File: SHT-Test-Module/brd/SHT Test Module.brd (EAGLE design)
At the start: 38.1 x 38.1 mm, 13 parts

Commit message: Added SHT board files
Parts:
- moved U$11 35.1 mm to (34.2, 15.2)
- moved U$6 29.2 mm to (31.5, 16.9)
- moved U$7 24.5 mm to (21.8, 5.21), turned to 270 degrees
- moved U$8 21.0 mm to (7.24, 13.8), turned to 270 degrees
- moved U$5 19.7 mm to (22.9, 29.1), turned to 90 degrees
- moved U$9 12.9 mm to (7.24, 17.8)
- moved U$1 6.45 mm to (13.6, 15.6), turned to 0 degrees
- moved U$2 5.66 mm to (28.8, 27.4)
- moved U$3 5.66 mm to (28.8, 24.9)
- moved U$4 5.66 mm to (28.8, 22.4)
- moved U$12 5.53 mm to (28.8, 30.1)
- moved U$10 3.75 mm to (20.1, 14.9), turned to 270 degrees
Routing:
- net GND: track 95.7 -> 24.7 mm, vias 5 -> 8
- net DATA: track 38.2 -> 19.5 mm
- net CMD: track 8.35 -> 20.3 mm, vias 0 -> 2
- net PING: track 12.5 -> 20.7 mm
- net SCK: track 16.7 -> 8.52 mm, vias 0 -> 1
- net CLK: track 25.0 -> 19.2 mm
- net SDA: track 19.0 -> 13.4 mm, vias 2 -> 0
- net MISO: track 14.9 -> 9.78 mm
- net ALIVE: track 17.0 -> 22.0 mm, vias 0 -> 2
- net RESET: track 62.0 -> 59.8 mm, vias 1 -> 3
- net N$12: track 8.65 -> 6.94 mm
- net N$15: track 8.27 -> 6.99 mm
- net N$14: track 8.27 -> 6.99 mm
- net N$13: track 8.27 -> 6.99 mm
- net SCL: track 16.0 -> 16.9 mm
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- added copper zone on layer 16, net GND
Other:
- board size 38.1 x 38.1 mm -> 38.1 x 38.2 mm

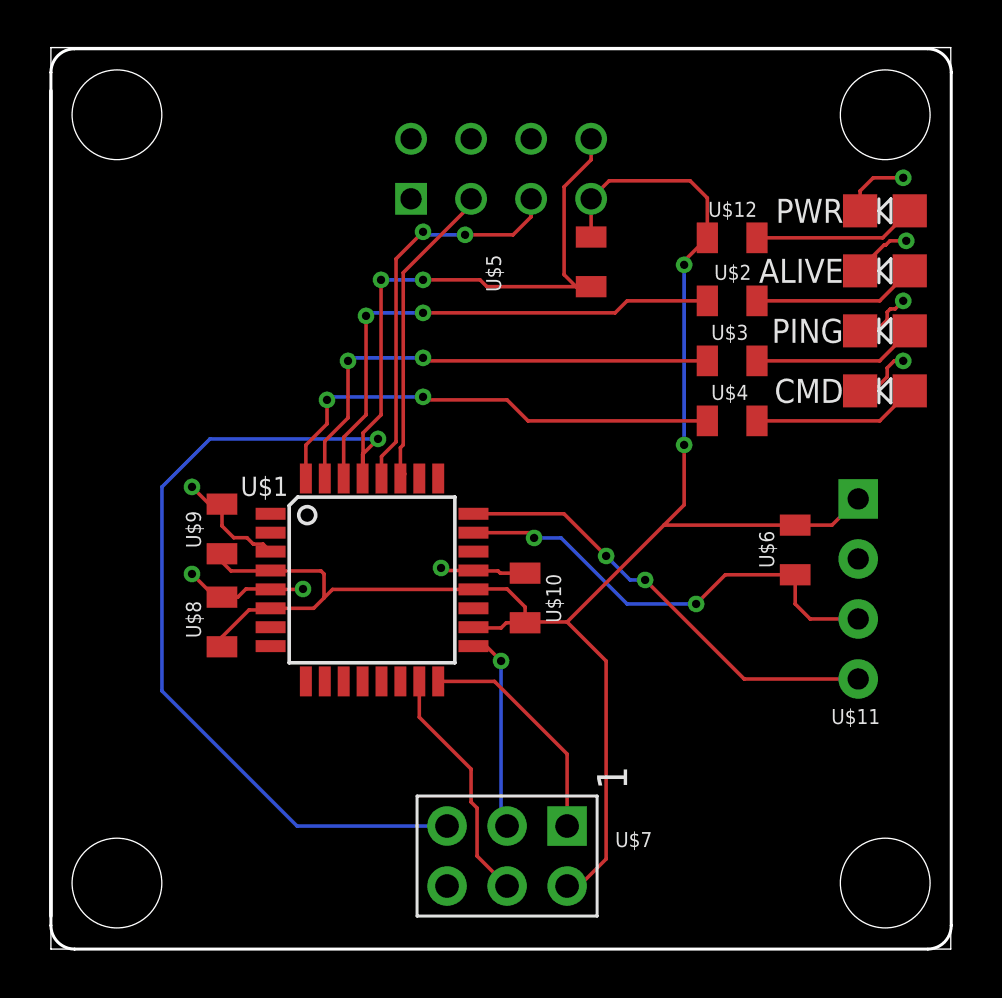
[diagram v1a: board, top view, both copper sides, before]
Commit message: updated board templates and modified existing boards to use the mk2 templates.
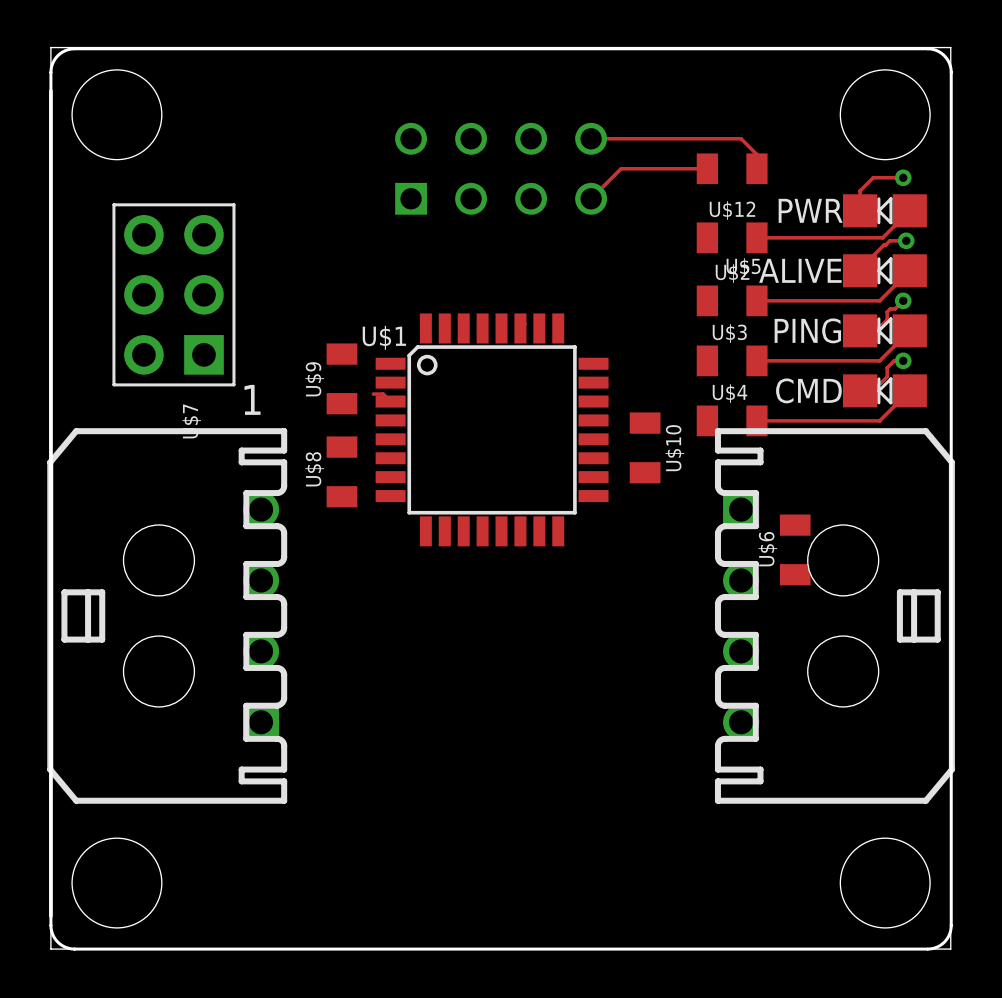
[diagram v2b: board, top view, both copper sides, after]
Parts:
- removed U$11: 4PIN-HEADER, 000_CustomPartsMaster:4HEADER_10MIL
- moved U$7 25.2 mm to (6.48, 25.1), turned to 180 degrees
- moved U$10 8.13 mm to (25.1, 21.2)
- moved U$8 8.13 mm to (12.3, 20.2)
- moved U$1 8.13 mm to (18.7, 22.0)
- moved U$9 8.13 mm to (12.3, 24.1)
- moved U$5 7.15 mm to (28.8, 33.0), turned to 180 degrees
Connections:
- new net 3P3V: TESTMOUDULE.3P3V@2, TESTMOUDULE.3P3V@3
- net CLK: now also TESTMOUDULE.DATA1@1, TESTMOUDULE.DATA1@2; no longer U$11.P$4
- net DATA: now also TESTMOUDULE.DATA0@1, TESTMOUDULE.DATA0@2; no longer U$11.P$3
- net GND: now also TESTMOUDULE.GND@1, TESTMOUDULE.GND@2, TESTMOUDULE.GND@3; no longer TESTMOUDULE.GND, U$11.P$2
- net POWER: now also TESTMOUDULE.3P3V@1; no longer TESTMOUDULE.3P3V, U$11.P$1
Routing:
- net POWER: track 74.2 -> 5.45 mm, vias 2 -> 0
- net RESET: track 59.8 -> 7.90 mm, vias 3 -> 0
- net ALIVE: track 22.0 -> 0.00 mm, vias 2 -> 0
- net PING: track 20.7 -> 0.00 mm, vias 2 -> 0
- net CMD: track 20.3 -> 0.00 mm, vias 2 -> 0
- net DATA: track 19.5 -> 0.00 mm, vias 2 -> 0
- net CLK: track 19.2 -> 0.00 mm, vias 2 -> 0
- net SCL: track 16.9 -> 0.00 mm, vias 2 -> 0
- net SDA: track 13.4 -> 0.28 mm
- net GND: track 24.7 -> 11.7 mm, vias 8 -> 4
- net MOSI: track 10.2 -> 0.00 mm
- net MISO: track 9.78 -> 0.00 mm
- net SCK: track 8.52 -> 0.00 mm, vias 1 -> 0
- removed copper zone on layer 16, net GND
